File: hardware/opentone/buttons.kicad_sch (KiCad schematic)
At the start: 9 parts

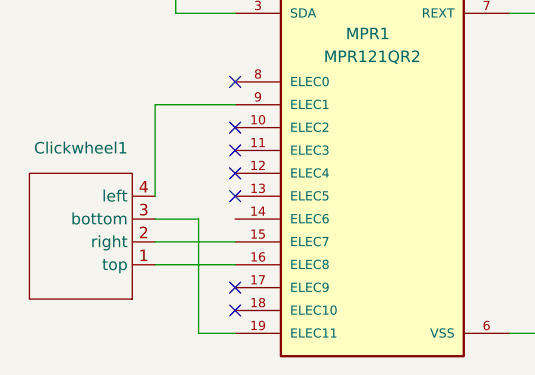
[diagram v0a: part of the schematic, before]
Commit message: Rename (#3)
* added dot when on a page with blank characters

* rename

* actions only on new version tag on master
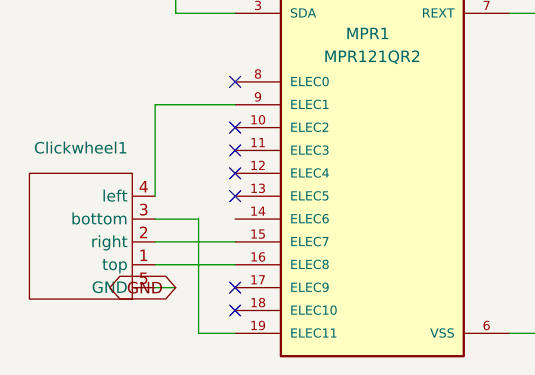
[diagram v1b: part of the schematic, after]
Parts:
- Clickwheel1: footprint openpod:clickwheel_1 -> opentone:clickwheel_1; symbol openpod:clickwheel -> opentone:clickwheel
- MPR1: footprint openpod:mpr121qr2 -> opentone:mpr121qr2; symbol openpod:MPR121QR2 -> opentone:MPR121QR2
- bottom1, center1, left1, right1, top1: footprint openpod:SW_SKQGAFE010 -> opentone:SW_SKQGAFE010; symbol openpod:SKQGAFE010 -> opentone:SKQGAFE010
- clickwheel-connector1, clickwheel-connector2: symbol openpod:clickwheel-connector -> opentone:clickwheel-connector
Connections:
- new net GND: Clickwheel1.5 (GND)
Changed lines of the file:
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@@
+	(wire
+		(pts
+			(xy 42.164 87.63) (xy 44.45 87.63)
+		)
+		(stroke
+			(width 0)
+			(type default)
+		)
+	)
 	(wire
 		(pts
@@
 		)
 	)
+	(global_label "GND"
+		(shape bidirectional)
+		(at 44.45 87.63 180)
+		(fields_autoplaced yes)
+		(effects
+			(font
+				(size 1.27 1.27)
+			)
+			(justify right)
+		)
+		(property "Intersheetrefs" "${INTERSHEET_REFS}"
+			(at 37.9 87.63 0)
+			(effects
+				(font
+					(size 1.27 1.27)
+				)
+				(justify right)
+				(hide yes)
+			)
+		)
+	)
 	(symbol
-		(lib_id "openpod:SKQGAFE010")
+		(lib_id "opentone:SKQGAFE010")
 		(at 143.256 42.926 0)
 		(unit 1)
@@
 			)
 		)
-		(property "Footprint" "openpod:SW_SKQGAFE010"
+		(property "Footprint" "opentone:SW_SKQGAFE010"
 			(at 143.256 42.926 0)
 			(effects
@@
 		)
 		(instances
-			(project "openpod"
+			(project "opentone"
 				(path "/0122bb8c-dbef-4db1-a6c6-9be780a38d9f/a2d473bc-020f-4f45-b688-c249a4b738f4"
 					(reference "top1")
@@
 	)
 	(symbol
-		(lib_id "openpod:SKQGAFE010")
+		(lib_id "opentone:SKQGAFE010")
 		(at 164.338 58.928 0)
 		(unit 1)
@@
 			)
 		)
-		(property "Footprint" "openpod:SW_SKQGAFE010"
+		(property "Footprint" "opentone:SW_SKQGAFE010"
 			(at 164.338 58.928 0)
 			(effects
@@
 		)
 		(instances
-			(project "openpod"
+			(project "opentone"
 				(path "/0122bb8c-dbef-4db1-a6c6-9be780a38d9f/a2d473bc-020f-4f45-b688-c249a4b738f4"
 					(reference "center1")
@@
 	)
 	(symbol
-		(lib_id "openpod:SKQGAFE010")
+		(lib_id "opentone:SKQGAFE010")
 		(at 165.1 41.91 0)
 		(unit 1)
@@
 			)
 		)
-		(property "Footprint" "openpod:SW_SKQGAFE010"
+		(property "Footprint" "opentone:SW_SKQGAFE010"
 			(at 165.1 41.91 0)
 			(effects
@@
 		)
 		(instances
-			(project "openpod"
+			(project "opentone"
 				(path "/0122bb8c-dbef-4db1-a6c6-9be780a38d9f/a2d473bc-020f-4f45-b688-c249a4b738f4"
 					(reference "bottom1")
@@
 	)
 	(symbol
-		(lib_id "openpod:clickwheel-connector")
+		(lib_id "opentone:clickwheel-connector")
 		(at 79.248 24.384 90)
 		(unit 1)
@@
 		)
 		(instances
-			(project "openpod"
+			(project "opentone"
 				(path "/0122bb8c-dbef-4db1-a6c6-9be780a38d9f/a2d473bc-020f-4f45-b688-c249a4b738f4"
 					(reference "clickwheel-connector1")
@@
 	)
 	(symbol
-		(lib_id "openpod:clickwheel")
+		(lib_id "opentone:clickwheel")
 		(at 34.544 82.55 180)
 		(unit 1)
@@
 			)
 		)
-		(property "Footprint" "openpod:clickwheel_1"
+		(property "Footprint" "opentone:clickwheel_1"
 			(at 34.544 80.01 0)
 			(effects
@@
 		(pin "4"
 		)
+		(pin "5"
+		)
 		(instances
-			(project "openpod"
+			(project "opentone"
 				(path "/0122bb8c-dbef-4db1-a6c6-9be780a38d9f/a2d473bc-020f-4f45-b688-c249a4b738f4"
 					(reference "Clickwheel1")
@@
 	)
 	(symbol
-		(lib_id "openpod:SKQGAFE010")
+		(lib_id "opentone:SKQGAFE010")
 		(at 183.896 42.672 0)
 		(unit 1)
@@
 			)
 		)
-		(property "Footprint" "openpod:SW_SKQGAFE010"
+		(property "Footprint" "opentone:SW_SKQGAFE010"
 			(at 183.896 42.672 0)
 			(effects
@@
 		)
 		(instances
-			(project "openpod"
+			(project "opentone"
 				(path "/0122bb8c-dbef-4db1-a6c6-9be780a38d9f/a2d473bc-020f-4f45-b688-c249a4b738f4"
 					(reference "left1")
@@
 	)
 	(symbol
-		(lib_id "openpod:SKQGAFE010")
+		(lib_id "opentone:SKQGAFE010")
 		(at 143.256 59.436 0)
 		(unit 1)
@@
 			)
 		)
-		(property "Footprint" "openpod:SW_SKQGAFE010"
+		(property "Footprint" "opentone:SW_SKQGAFE010"
 			(at 143.256 59.436 0)
 			(effects
@@
 		)
 		(instances
-			(project "openpod"
+			(project "opentone"
 				(path "/0122bb8c-dbef-4db1-a6c6-9be780a38d9f/a2d473bc-020f-4f45-b688-c249a4b738f4"
 					(reference "right1")
@@
 	)
 	(symbol
-		(lib_id "openpod:MPR121QR2")
+		(lib_id "opentone:MPR121QR2")
 		(at 66.294 69.85 0)
 		(unit 1)
@@
 			)
 		)
-		(property "Footprint" "openpod:mpr121qr2"
+		(property "Footprint" "opentone:mpr121qr2"
 			(at 66.294 69.85 0)
 			(effects
@@
 		)
 		(instances
-			(project "openpod"
+			(project "opentone"
 				(path "/0122bb8c-dbef-4db1-a6c6-9be780a38d9f/a2d473bc-020f-4f45-b688-c249a4b738f4"
 					(reference "MPR1")
@@
 	)
 	(symbol
-		(lib_id "openpod:clickwheel-connector")
+		(lib_id "opentone:clickwheel-connector")
 		(at 123.19 74.422 90)
 		(unit 1)
@@
 		)
 		(instances
-			(project "openpod"
+			(project "opentone"
 				(path "/0122bb8c-dbef-4db1-a6c6-9be780a38d9f/a2d473bc-020f-4f45-b688-c249a4b738f4"
 					(reference "clickwheel-connector2")
